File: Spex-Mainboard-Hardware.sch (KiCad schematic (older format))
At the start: 38 parts, among them P1 USB_OTG, P14 CONN_01X02, P2 SWD Header, SW1 SW_PUSH, SW2 SW_PUSH, U1 MKL02Z32VFG4, U14 AT45DB641E, U2 NUP2201MR6, U3 MK20DX256VLH7, U4 NUP2201MR6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

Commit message: small update
getting ready to order PCB's, making sure they are good to go.
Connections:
- no-connect marks 10 -> 25

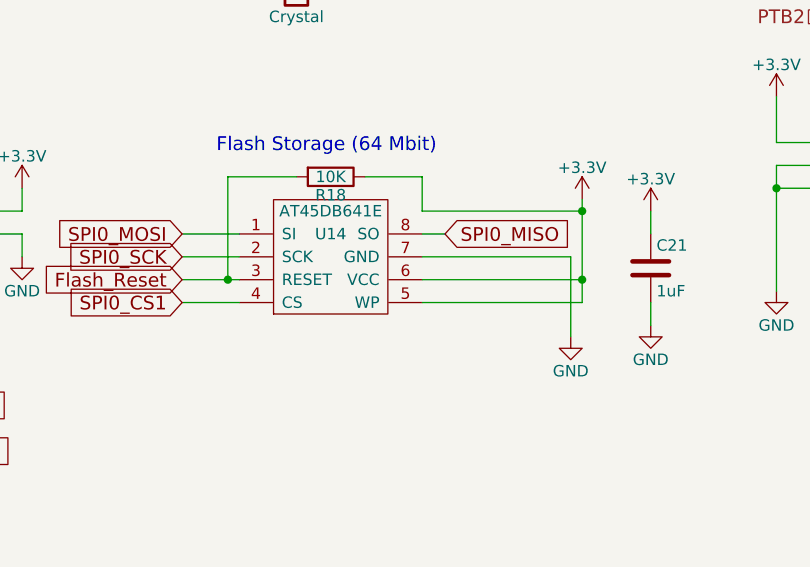
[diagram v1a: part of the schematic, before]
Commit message: small update round 2
cleaning up PCB, adding SPI CS pullup resistors
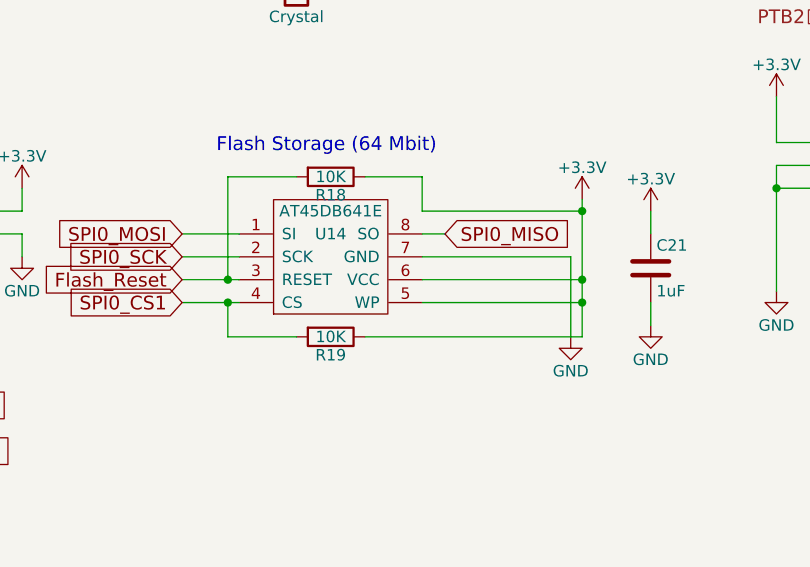
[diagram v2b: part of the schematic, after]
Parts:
- added R19: 10K, Resistors_SMD:R_0603, symbol R
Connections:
- net +3V3: now also R19.1
- net SPI0_CS1: now also R19.2
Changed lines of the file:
@@
 	6400 5800 5700 5800
 Wire Wire Line
-	6400 5450 6400 5900
+	6400 5450 6400 6050
 $Comp
 L +3.3V #PWR033
@@
 NoConn ~ 4550 2200
 NoConn ~ 4550 1800
+$Comp
+L R R19
+U 1 1 580804F8
+P 5300 6050
+F 0 "R19" V 5380 6050 50  0000 C CNN
+F 1 "10K" V 5300 6050 50  0000 C CNN
+F 2 "Resistors_SMD:R_0603" V 5230 6050 50  0001 C CNN
+F 3 "" H 5300 6050 50  0000 C CNN
+	1    5300 6050
+	0    1    1    0
+$EndComp
+Wire Wire Line
+	6400 6050 5450 6050
+Connection ~ 6400 5900
+Wire Wire Line
+	5150 6050 4850 6050
+Wire Wire Line
+	4850 6050 4850 5900
+Connection ~ 4850 5900
 $EndSCHEMATC

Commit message: removed SPI Flash, minor changes, updated Kicad
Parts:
- removed C21: 1uF, Capacitors_SMD:C_0603, symbol C
- removed R18, R19: 10K, Resistors_SMD:R_0603, symbol R
- removed U14: AT45DB641E, SMD_Packages:SOIC-8-N, symbol AT45DB641E
- D1, D2, D3, D4: symbol LED -> LED-RESCUE-Spex-Mainboard-Hardware
- P1: symbol USB_OTG -> USB_OTG-RESCUE-Spex-Mainboard-Hardware
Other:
- note removed: "Flash Storage (64 Mbit)"
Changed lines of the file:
@@
 $EndComp
 $Comp
-L USB_OTG P1
+L USB_OTG-RESCUE-Spex-Mainboard-Hardware P1
 U 1 1 56581306
 P 2200 1750
@@
 $EndComp
 $Comp
-L LED D1
+L LED-RESCUE-Spex-Mainboard-Hardware D1
 U 1 1 56DC1E42
 P 1950 2300
@@
 $EndComp
 $Comp
-L LED D2
+L LED-RESCUE-Spex-Mainboard-Hardware D2
 U 1 1 56ECA2DA
 P 7500 1750
@@
 $EndComp
 $Comp
-L LED D3
+L LED-RESCUE-Spex-Mainboard-Hardware D3
 U 1 1 56ECA423
 P 7750 1750
@@
 $EndComp
 $Comp
-L LED D4
+L LED-RESCUE-Spex-Mainboard-Hardware D4
 U 1 1 56ECA578
 P 8000 1750
@@
 	0    1    1    0
 $EndComp
-Text GLabel 4650 5600 0    60   Input ~ 0
-SPI0_MOSI
-Text GLabel 5800 5600 2    60   Input ~ 0
-SPI0_MISO
-Text GLabel 4650 5700 0    60   Input ~ 0
-SPI0_SCK
 Text GLabel 3100 5350 2    60   Input ~ 0
 SPI0_CS0
@@
 Text GLabel 6300 2900 2    60   Input ~ 0
 SPI0_CS1
-$Comp
-L AT45DB641E U14
-U 1 1 56FB6452
-P 5300 5800
-F 0 "U14" H 5300 6000 50  0000 C CNN
-F 1 "AT45DB641E" H 5300 6100 50  0000 C CNN
-F 2 "SMD_Packages:SOIC-8-N" H 5450 5600 50  0001 C CNN
-F 3 "DOCUMENTATION" H 5300 5500 50  0001 C CNN
-	1    5300 5800
-	1    0    0    -1
-$EndComp
-$Comp
-L +3.3V #PWR031
-U 1 1 56FB6BAF
-P 6400 5450
-F 0 "#PWR031" H 6400 5300 50  0001 C CNN
-F 1 "+3.3V" H 6400 5590 50  0000 C CNN
-F 2 "" H 6400 5450 60  0000 C CNN
-F 3 "" H 6400 5450 60  0000 C CNN
-	1    6400 5450
-	1    0    0    -1
-$EndComp
-$Comp
-L GND #PWR032
-U 1 1 56FB6D46
-P 6350 6050
-F 0 "#PWR032" H 6350 5800 50  0001 C CNN
-F 1 "GND" H 6350 5900 50  0000 C CNN
-F 2 "" H 6350 6050 60  0000 C CNN
-F 3 "" H 6350 6050 60  0000 C CNN
-	1    6350 6050
-	1    0    0    -1
-$EndComp
-$Comp
-L C C21
-U 1 1 56FB76C9
-P 6700 5750
-F 0 "C21" H 6725 5850 50  0000 L CNN
-F 1 "1uF" H 6725 5650 50  0000 L CNN
-F 2 "Capacitors_SMD:C_0603" H 6738 5600 50  0001 C CNN
-F 3 "" H 6700 5750 50  0000 C CNN
-	1    6700 5750
-	1    0    0    -1
-$EndComp
 Wire Wire Line
 	1350 900  2100 900
@@
 Wire Wire Line
 	6300 3100 5750 3100
-Wire Wire Line
-	5700 5700 6350 5700
-Wire Wire Line
-	6350 5700 6350 6050
-Wire Wire Line
-	6400 5800 5700 5800
-Wire Wire Line
-	6400 5450 6400 6050
-$Comp
-L +3.3V #PWR033
-U 1 1 56FB887E
-P 6700 5500
-F 0 "#PWR033" H 6700 5350 50  0001 C CNN
-F 1 "+3.3V" H 6700 5640 50  0000 C CNN
-F 2 "" H 6700 5500 60  0000 C CNN
-F 3 "" H 6700 5500 60  0000 C CNN
-	1    6700 5500
-	1    0    0    -1
-$EndComp
-$Comp
-L GND #PWR034
-U 1 1 56FB8A18
-P 6700 6000
-F 0 "#PWR034" H 6700 5750 50  0001 C CNN
-F 1 "GND" H 6700 5850 50  0000 C CNN
-F 2 "" H 6700 6000 60  0000 C CNN
-F 3 "" H 6700 6000 60  0000 C CNN
-	1    6700 6000
-	1    0    0    -1
-$EndComp
-Wire Wire Line
-	6700 5600 6700 5500
-Wire Wire Line
-	6700 5900 6700 6000
-Text GLabel 4650 5900 0    60   Input ~ 0
-SPI0_CS1
-Wire Wire Line
-	4650 5900 4900 5900
 Text GLabel 3100 5050 2    60   Input ~ 0
 SPI0_MOSI
@@
 Text GLabel 3100 5250 2    60   Input ~ 0
 SPI0_SCK
-Wire Wire Line
-	4650 5600 4900 5600
-Wire Wire Line
-	4650 5700 4900 5700
-Wire Wire Line
-	5800 5600 5700 5600
-Text Notes 4800 5250 0    60   ~ 0
-Flash Storage (64 Mbit)
 $Comp
 L +5V #PWR035
@@
 Wire Wire Line
 	9550 3600 9700 3600
-Wire Wire Line
-	6400 5900 5700 5900
-Connection ~ 6400 5800
 Text GLabel 6300 3200 2    60   Input ~ 0
 Flash_Reset
-Text GLabel 4650 5800 0    60   Input ~ 0
-Flash_Reset
-Wire Wire Line
-	4650 5800 4900 5800
 Wire Wire Line
 	6300 3200 5750 3200
-$Comp
-L R R18
-U 1 1 5709182B
-P 5300 5350
-F 0 "R18" V 5380 5350 50  0000 C CNN
-F 1 "10K" V 5300 5350 50  0000 C CNN
-F 2 "Resistors_SMD:R_0603" V 5230 5350 50  0001 C CNN
-F 3 "" H 5300 5350 50  0000 C CNN
-	1    5300 5350
-	0    1    1    0
-$EndComp
-Wire Wire Line
-	5150 5350 4850 5350
-Wire Wire Line
-	4850 5350 4850 5800
-Connection ~ 4850 5800
-Wire Wire Line
-	5450 5350 5700 5350
-Wire Wire Line
-	5700 5350 5700 5500
-Wire Wire Line
-	5700 5500 6400 5500
-Connection ~ 6400 5500
 Text GLabel 6350 4100 2    60   Input ~ 0
 RESET_b
@@
 NoConn ~ 4550 2200
 NoConn ~ 4550 1800
-$Comp
-L R R19
-U 1 1 580804F8
-P 5300 6050
-F 0 "R19" V 5380 6050 50  0000 C CNN
-F 1 "10K" V 5300 6050 50  0000 C CNN
-F 2 "Resistors_SMD:R_0603" V 5230 6050 50  0001 C CNN
-F 3 "" H 5300 6050 50  0000 C CNN
-	1    5300 6050
-	0    1    1    0
-$EndComp
-Wire Wire Line
-	6400 6050 5450 6050
-Connection ~ 6400 5900
-Wire Wire Line
-	5150 6050 4850 6050
-Wire Wire Line
-	4850 6050 4850 5900
-Connection ~ 4850 5900
 $EndSCHEMATC
